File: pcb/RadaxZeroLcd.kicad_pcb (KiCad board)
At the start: 2 copper layers, 84.8 x 45.5 mm, 7 parts, among them J1 RadaxZero, J2 4.0inch LCD, J3 UART, J4 I2C, J5 SYS UART

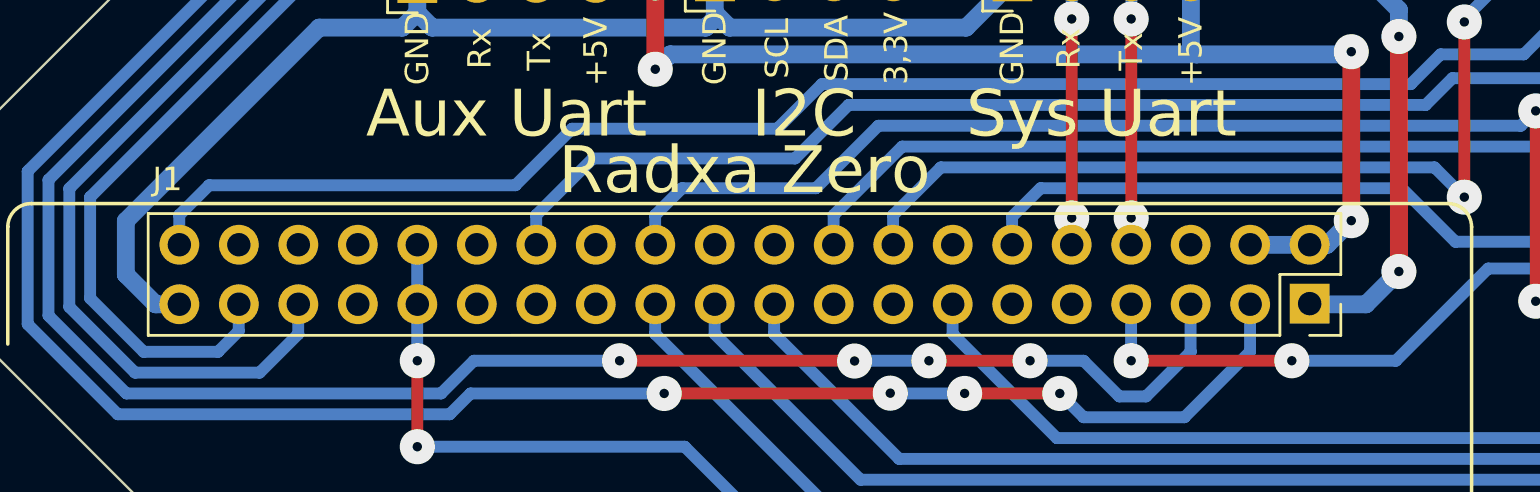
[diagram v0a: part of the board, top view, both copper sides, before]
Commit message: update radxa zero footprint
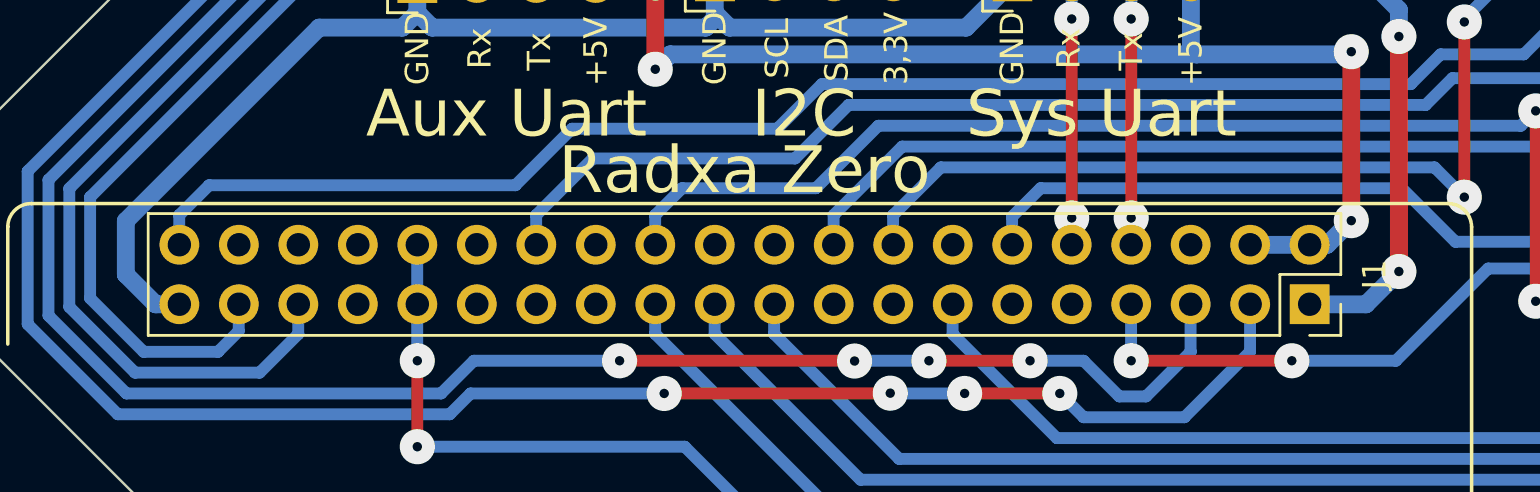
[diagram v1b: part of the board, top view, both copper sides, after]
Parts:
- J1: footprint Connector_PinHeader_2.54mm:PinHeader_2x20_P2.54mm_Vertical -> Connector_PinSocket_2.54mm:PinSocket_2x20_P2.54mm_Vertical
- moved J1 2.54 mm to (116.6, 98.3)
